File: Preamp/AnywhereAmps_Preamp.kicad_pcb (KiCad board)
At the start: 2 copper layers, 69.1 x 45.2 mm, 59 parts, among them J1 +9V, J2 Battery, J3 VCC, J4 Switch, J5 Pwr LED, J6 POTI, J7 Audio_In, J8 Audio_Out, U1 PTPSM5601R5H, U2 MAX17562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

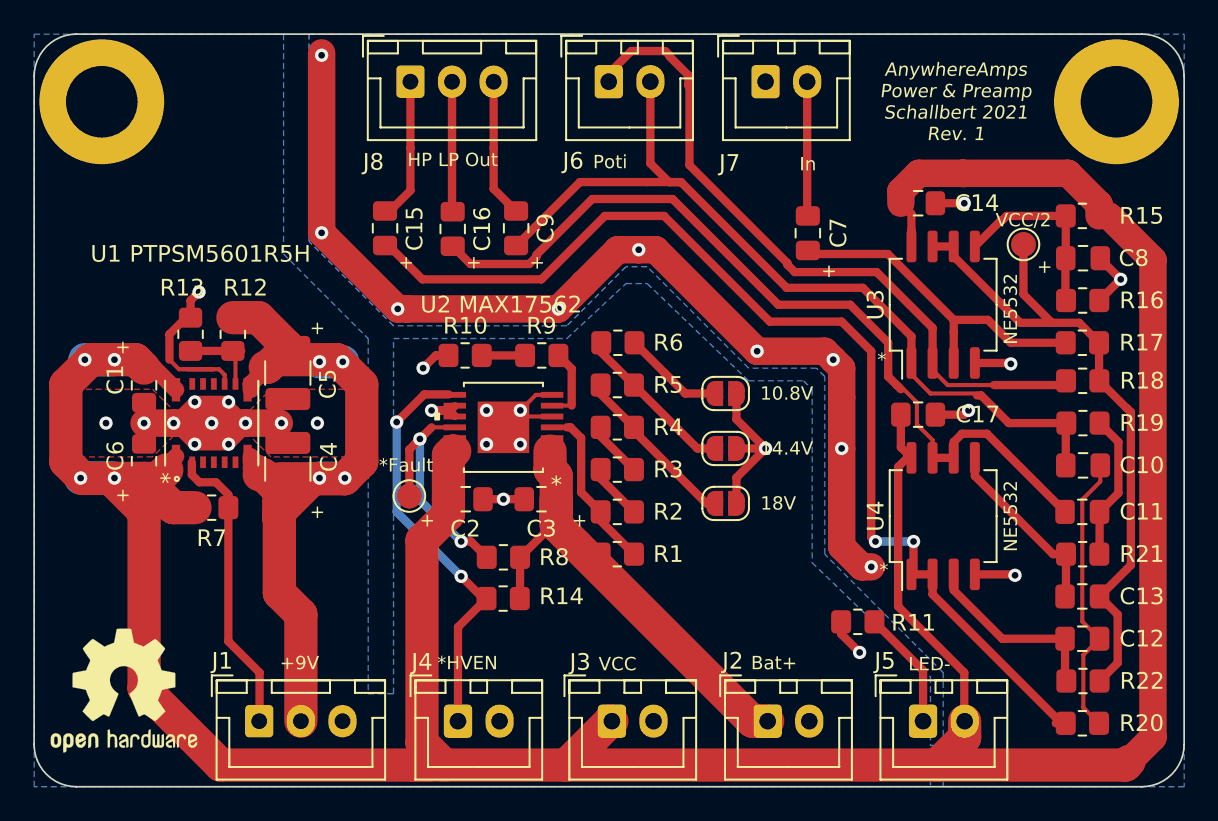
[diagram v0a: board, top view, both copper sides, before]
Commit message: - fine-tune component placement - add batt and VCC copper layers - update SilkScreen
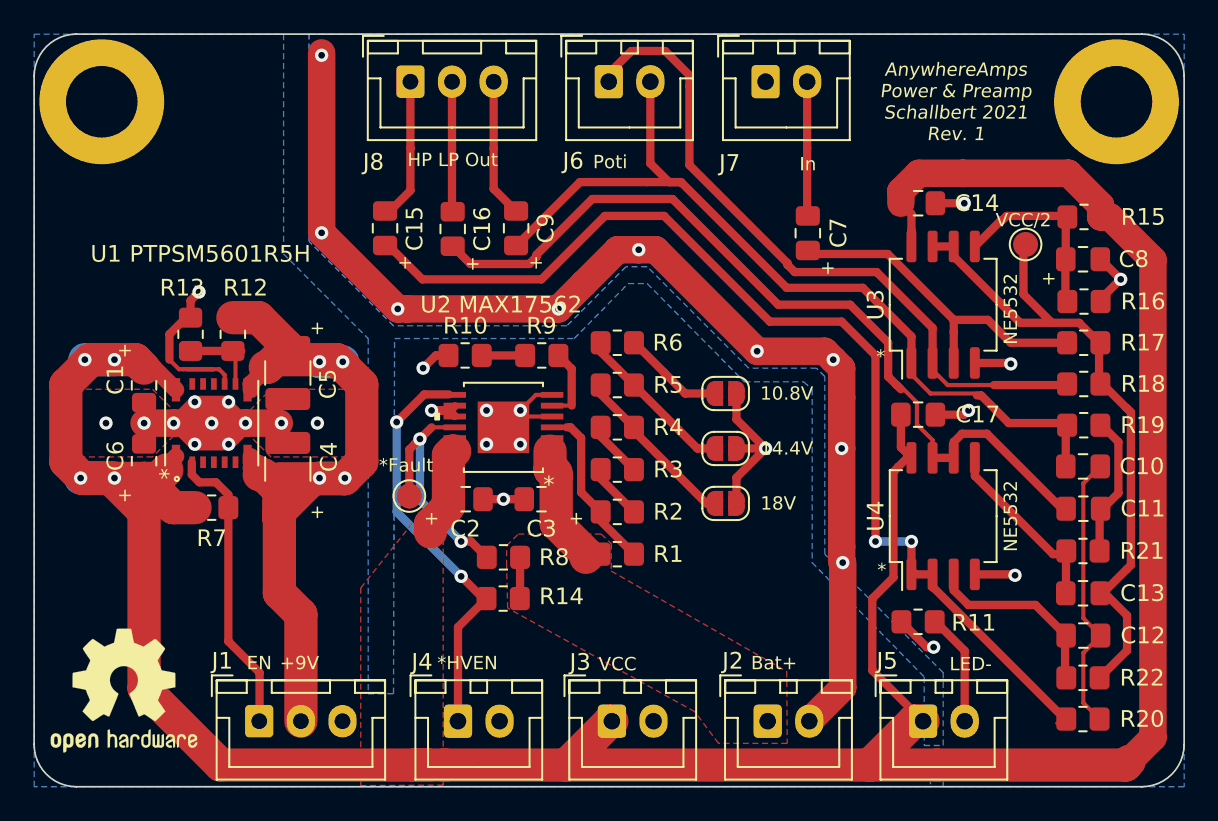
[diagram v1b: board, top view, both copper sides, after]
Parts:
- moved R11 3.62 mm to (154.4, 136.9)
- moved R20 0.26 mm to (164.4, 142.7)
- moved R18 0.20 mm to (164.4, 122.6)
- moved C11 0.20 mm to (164.4, 130.1)
- moved C12 0.20 mm to (164.4, 137.7)
- moved C13 0.20 mm to (164.4, 135.2)
- moved R21 0.19 mm to (164.4, 132.7)
- moved R22 0.19 mm to (164.4, 140.3)
- moved R19 0.14 mm to (164.4, 125.1)
- moved TP2 0.13 mm to (160.9, 114.2)
- moved R15 0.11 mm to (164.4, 112.6)
- moved R16 0.10 mm to (164.4, 117.7)
- moved R17 0.08 mm to (164.4, 120.1)
- moved C10 0.06 mm to (164.4, 127.6)
- moved C8 0.06 mm to (164.4, 115.1)
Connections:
- J5 pad 1: Net-(J5-Pad1) -> VCC
- J5 pad 2: VCC -> Net-(J5-Pad2)
- R11 pad 2: Net-(J5-Pad1) -> Net-(J5-Pad2)
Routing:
- net +BATT: track 29.5 -> 10.3 mm
- net VCC: track 208.9 -> 195.9 mm
- net GND: track 136.9 -> 146.1 mm
- net Net-(J5-Pad1): track 8.00 -> 0.00 mm
- net Net-(J5-Pad2): track 0.00 -> 6.79 mm
- net Net-(C15-Pad1): track 67.3 -> 66.6 mm
- net GNDA: track 41.4 -> 42.0 mm
- added copper zone on F.Cu, net +BATT
- added copper zone on F.Cu, net VCC
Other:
- board text added: "EN"

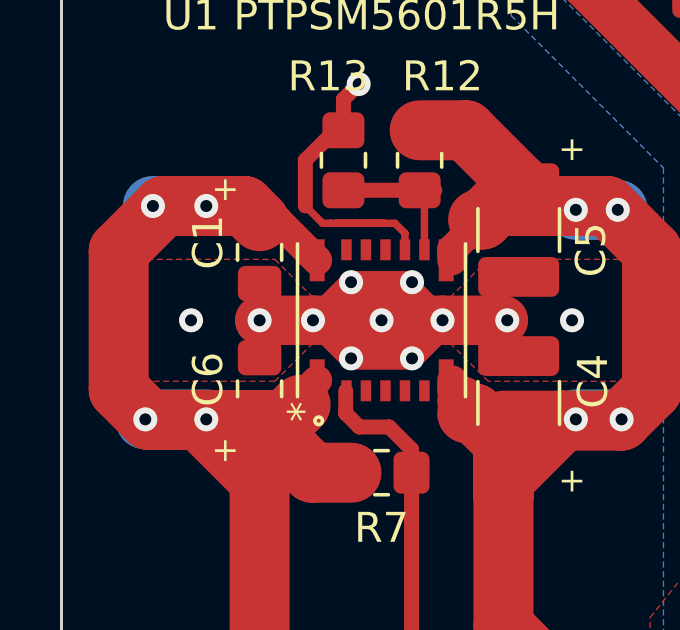
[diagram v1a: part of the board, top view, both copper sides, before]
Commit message: - update 1.25k resistors to 1.2k resistors
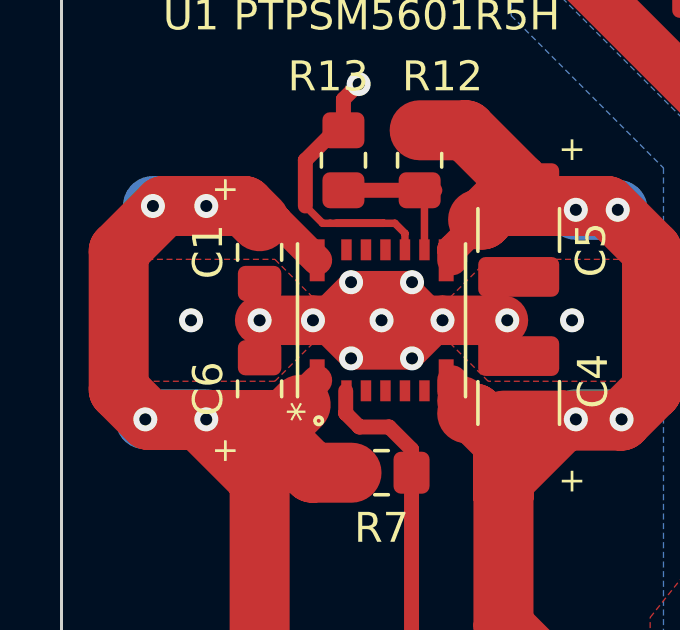
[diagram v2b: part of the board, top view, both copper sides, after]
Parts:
- R10, R11, R13, R9: value 1.25k -> 1.2k
- turned C1 to 270 degrees
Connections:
- C1 pad 1: GND -> VCC
- C1 pad 2: VCC -> GND
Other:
- board text added: "33n MLCC C10, C11, C12, C13, C14, C17 4.7u low ESR Tantalum C1, C2, C3, C6, C7, C8, C9, C15, C16 47u low ESR Tantalum C4, C5 390k R1, R7, R8, R14 10k R2, R3, R4, R5, R6, R12, R15, R16, R17, R18, R19, R20, R21, R22 1.2k R9, R10, R11, R13"
- board text removed: "33n MLCC C10, C11, C12, C13, C14, C17 4.7u low ESR Tantalum C1, C2, C3, C6, C7, C8, C9, C15, C16 47u low ESR Tantalum C4, C5 390k R1, R7, R8, R14 10k R2, R3, R4, R5, R6, R12, R15, R16, R17, R18, R19, R20, R21, R22 1.25k R9, R10, R11, R13"
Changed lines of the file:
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@@
     (tags "capacitor handsolder")
     (attr smd)
-    (fp_text reference C6 (at 0.3175 -1.7145 90) (layer F.SilkS)
+    (fp_text reference C6 (at 0 -1.7145 90) (layer F.SilkS)
       (effects (font (size 1 1) (thickness 0.15)))
     )
@@
   )
   (module Capacitor_SMD:C_0805_2012Metric_Pad1.18x1.45mm_HandSolder (layer Front)
-    (at 107.95 122.7035 90)
+    (at 107.95 122.7035 270)
     (descr "Capacitor SMD 0805 (2012 Metric), square (rectangular) end terminal, IPC_7351 nominal with elongated pad for handsoldering. (Body size source: IPC-SM-782 page 76, https://www.pcb-3d.com/wordpress/wp-content/uploads/ipc-sm-782a_amendment_1_and_2.pdf, https://docs.google.com/spreadsheets/d/1BsfQQcO9C6DZCsRaXUlFlo91Tg2WpOkGARC1WS5S8t0/edit?usp=sharing), generated with kicad-footprint-generator")
     (tags "capacitor handsolder")
     (attr smd)
-    (fp_text reference C1 (at 0.339 -1.7145 90) (layer F.SilkS)
+    (fp_text reference C1 (at -0.0215 1.7145 90) (layer F.SilkS)
       (effects (font (size 1 1) (thickness 0.15)))
     )
@@
       (effects (font (size 0.5 0.5) (thickness 0.08)))
     )
-    (pad 2 smd roundrect (at 1.0375 0 90) (size 1.175 1.45) (layers Front F.Paste F.Mask) (roundrect_rratio 0.212766)
+    (pad 2 smd roundrect (at 1.0375 0 270) (size 1.175 1.45) (layers Front F.Paste F.Mask) (roundrect_rratio 0.212766)
+      (net 2 GND))
+    (pad 1 smd roundrect (at -1.0375 0 270) (size 1.175 1.45) (layers Front F.Paste F.Mask) (roundrect_rratio 0.212766)
       (net 1 VCC))
-    (pad 1 smd roundrect (at -1.0375 0 90) (size 1.175 1.45) (layers Front F.Paste F.Mask) (roundrect_rratio 0.212766)
-      (net 2 GND))
     (model ${KISYS3DMOD}/Capacitor_SMD.3dshapes/C_0805_2012Metric.wrl
       (at (xyz 0 0 0))
@@
       (effects (font (size 1 1) (thickness 0.15)))
     )
-    (fp_text value 1.25k (at 0 1.65) (layer F.Fab)
+    (fp_text value 1.2k (at 0 1.65) (layer F.Fab)
       (effects (font (size 1 1) (thickness 0.15)))
     )
@@
       (effects (font (size 1 1) (thickness 0.15)))
     )
-    (fp_text value 1.25k (at 0 1.65) (layer F.Fab)
+    (fp_text value 1.2k (at 0 1.65) (layer F.Fab)
       (effects (font (size 1 1) (thickness 0.15)))
     )
@@
       (effects (font (size 1 1) (thickness 0.15)))
     )
-    (fp_text value 1.25k (at 0 1.65) (layer F.Fab)
+    (fp_text value 1.2k (at 0 1.65) (layer F.Fab)
       (effects (font (size 1 1) (thickness 0.15)))
     )
@@
       (effects (font (size 1 1) (thickness 0.15)))
     )
-    (fp_text value 1.25k (at 0 1.65 90) (layer F.Fab)
+    (fp_text value 1.2k (at 0 1.65 90) (layer F.Fab)
       (effects (font (size 1 1) (thickness 0.15)))
     )
@@
     (effects (font (size 0.8 0.8) (thickness 0.1)))
   )
-  (gr_text "33n MLCC C10, C11, C12, C13, C14, C17\n4.7u low ESR Tantalum C1, C2, C3, C6, C7, C8, C9, C15, C16\n47u low ESR Tantalum C4, C5\n390k R1, R7, R8, R14\n10k R2, R3, R4, R5, R6, R12, R15, R16, R17, R18, R19, R20, R21, R22\n1.25k R9, R10, R11, R13" (at 169.418 116.586) (layer B.SilkS)
+  (gr_text "33n MLCC C10, C11, C12, C13, C14, C17\n4.7u low ESR Tantalum C1, C2, C3, C6, C7, C8, C9, C15, C16\n47u low ESR Tantalum C4, C5\n390k R1, R7, R8, R14\n10k R2, R3, R4, R5, R6, R12, R15, R16, R17, R18, R19, R20, R21, R22\n1.2k R9, R10, R11, R13" (at 169.418 116.586) (layer B.SilkS)
     (effects (font (size 0.8 0.8) (thickness 0.1)) (justify left mirror))
   )
